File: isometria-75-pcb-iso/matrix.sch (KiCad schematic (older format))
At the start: 252 parts, among them SW201 Rotary_Encoder_Switch

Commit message: major schematic/pcb rework
rewired SPI, added SPI CS/IRQ/RES pins, rewired part of the matrix in the process
changed to a larger header for SPI
added a divider for input voltage sensing
removed extension header due to a lack of remaining unused GPIOs
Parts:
- R283, R284: footprint Resistor_SMD:R_0603_1608Metric -> Resistor_SMD:R_0402_1005Metric
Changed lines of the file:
@@
 Connection ~ 9850 4850
 $Comp
-L power:GND #PWR0119
+L power:GND #PWR0121
 U 1 1 63289F50
 P 10850 1200
-F 0 "#PWR0119" H 10850 950 50  0001 C CNN
+F 0 "#PWR0121" H 10850 950 50  0001 C CNN
 F 1 "GND" H 10855 1027 50  0000 C CNN
 F 2 "" H 10850 1200 50  0001 C CNN
@@
 F 0 "R283" H 10350 1100 50  0000 L CNN
 F 1 "10k" H 10350 1000 50  0000 L CNN
-F 2 "Resistor_SMD:R_0603_1608Metric" H 10300 1000 50  0001 C CNN
+F 2 "Resistor_SMD:R_0402_1005Metric" H 10300 1000 50  0001 C CNN
 F 3 "~" H 10300 1000 50  0001 C CNN
 	1    10300 1000
@@
 F 0 "R284" H 10350 1400 50  0000 L CNN
 F 1 "10k" H 10350 1300 50  0000 L CNN
-F 2 "Resistor_SMD:R_0603_1608Metric" H 10300 1400 50  0001 C CNN
+F 2 "Resistor_SMD:R_0402_1005Metric" H 10300 1400 50  0001 C CNN
 F 3 "~" H 10300 1400 50  0001 C CNN
 	1    10300 1400
@@
 	10300 800  10300 900
 $Comp
-L power:+3.3V #PWR0120
+L power:+3.3V #PWR0122
 U 1 1 637D2133
 P 11000 800
-F 0 "#PWR0120" H 11000 650 50  0001 C CNN
+F 0 "#PWR0122" H 11000 650 50  0001 C CNN
 F 1 "+3.3V" H 11015 973 50  0000 C CNN
 F 2 "" H 11000 800 50  0001 C CNN

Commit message: final touches
changed some 0603 to 0402 for consistency, added vias to properly better ground planes, added LCSC part numbers for jlcpcb assembly
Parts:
- C201, C202: LCSC (none) -> C1525
- D201, D202, D203, D204, D205, D206, D207, D208, D209, D210, D211, D212, D213, D214, D215, D216, D217, D218, D219, D220, D221, D222, D223, D224, D225, D226, D227, D228, D229, D230, D231, D232, D233, D234, D235, D236, D237, D238, D239, D240, D241, D242, D243, D244, D245, D246, D247, D248, D249, D250, D251, D252, D253, D254, D255, D256, D257, D258, D259, D260, D261, D262, D263, D264, D265, D266, D267, D268, D269, D270, D271, D272, D273, D274, D275, D276, D277, D278, D279, D280, D281, D282, D283: LCSC (none) -> C2128
- MX201, MX202, MX203, MX204, MX205, MX206, MX207, MX208, MX209, MX210, MX211, MX212, MX213, MX214, MX215, MX216, MX217, MX218, MX219, MX220, MX221, MX222, MX223, MX224, MX225, MX226, MX227, MX228, MX229, MX230, MX231, MX232, MX233, MX234, MX235, MX236, MX237, MX238, MX239, MX240, MX241, MX242, MX243, MX244, MX245, MX246, MX247, MX248, MX249, MX250, MX251, MX252, MX253, MX254, MX255, MX256, MX257, MX258, MX259, MX260, MX261, MX262, MX263, MX264, MX265, MX266, MX267, MX268, MX269, MX270, MX271, MX272, MX273, MX274, MX275, MX276, MX277, MX278, MX279, MX280, MX281, MX282, SW201: LCSC (none) -> /
- R201, R202, R203, R204, R205, R206, R207, R208, R209, R210, R211, R212, R213, R214, R215, R216, R217, R218, R219, R220, R221, R222, R223, R224, R225, R226, R227, R228, R229, R230, R231, R232, R233, R234, R235, R236, R237, R238, R239, R240, R241, R242, R243, R244, R245, R246, R247, R248, R249, R250, R251, R252, R253, R254, R255, R256, R257, R258, R259, R260, R261, R262, R263, R264, R265, R266, R267, R268, R269, R270, R271, R272, R273, R274, R275, R276, R277, R278, R279, R280, R281, R282: LCSC (none) -> C23228
- R283, R284: LCSC (none) -> C25744

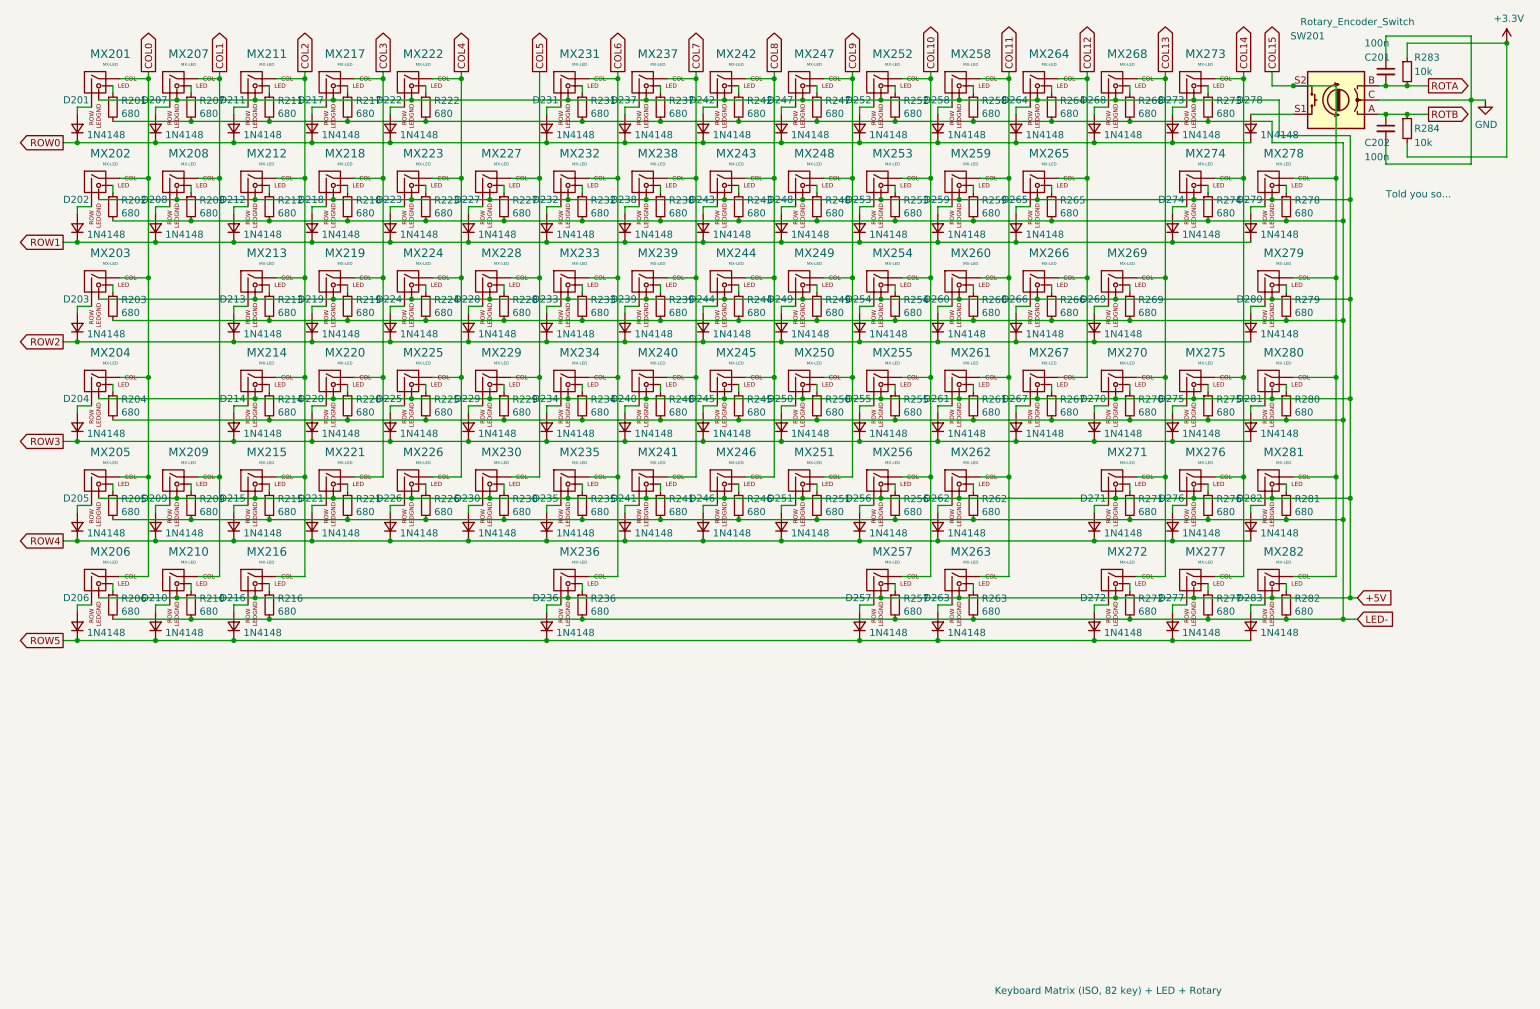
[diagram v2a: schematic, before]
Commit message: improved componend value formatting
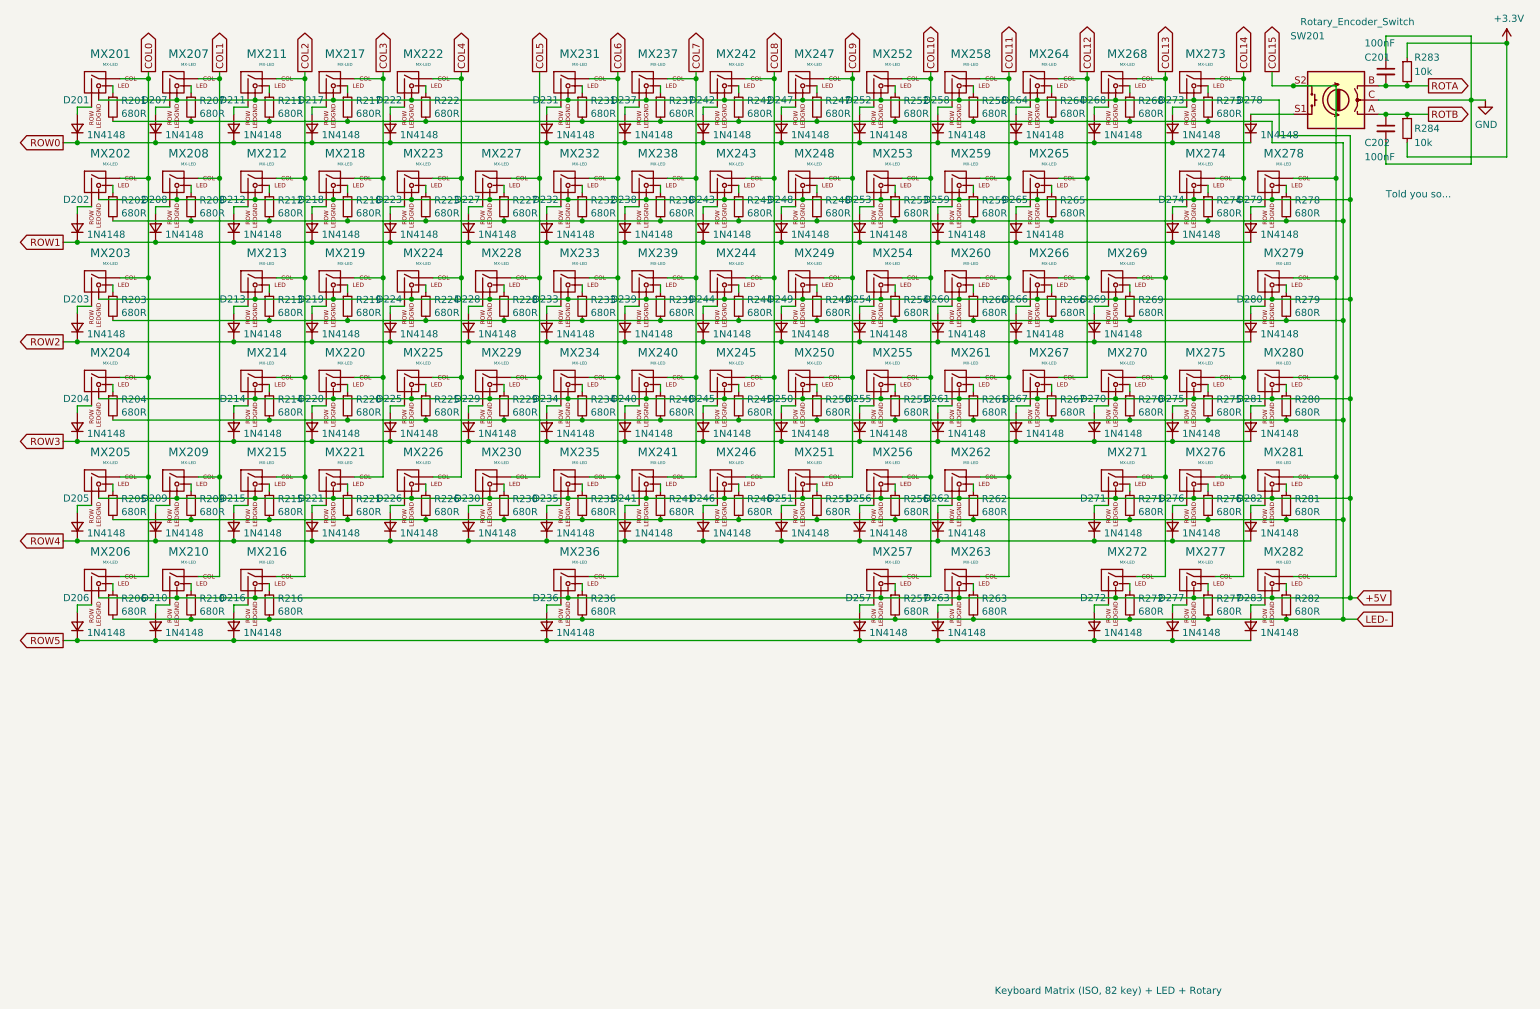
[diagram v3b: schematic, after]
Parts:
- C201, C202: value 100n -> 100nF
- MX201, MX202, MX203, MX204, MX205, MX206, MX207, MX208, MX209, MX210, MX211, MX212, MX213, MX214, MX215, MX216, MX217, MX218, MX219, MX220, MX221, MX222, MX223, MX224, MX225, MX226, MX227, MX228, MX229, MX230, MX231, MX232, MX233, MX234, MX235, MX236, MX237, MX238, MX239, MX240, MX241, MX242, MX243, MX244, MX245, MX246, MX247, MX248, MX249, MX250, MX251, MX252, MX253, MX254, MX255, MX256, MX257, MX258, MX259, MX260, MX261, MX262, MX263, MX264, MX265, MX266, MX267, MX268, MX269, MX270, MX271, MX272, MX273, MX274, MX275, MX276, MX277, MX278, MX279, MX280, MX281, MX282, SW201: LCSC / -> (none)
- R201, R202, R203, R204, R205, R206, R207, R208, R209, R210, R211, R212, R213, R214, R215, R216, R217, R218, R219, R220, R221, R222, R223, R224, R225, R226, R227, R228, R229, R230, R231, R232, R233, R234, R235, R236, R237, R238, R239, R240, R241, R242, R243, R244, R245, R246, R247, R248, R249, R250, R251, R252, R253, R254, R255, R256, R257, R258, R259, R260, R261, R262, R263, R264, R265, R266, R267, R268, R269, R270, R271, R272, R273, R274, R275, R276, R277, R278, R279, R280, R281, R282: value 680 -> 680R
